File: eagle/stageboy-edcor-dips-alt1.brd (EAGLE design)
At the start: 120 x 75 mm, 35 parts, among them IC1 MEGA8-P, IC2 7805TV, J1 POWER_JACKPTH, Q1 16MHz, X1 MIDI IN, X2 MIDI OUT, X4 22-23-2021, X6 GBIO

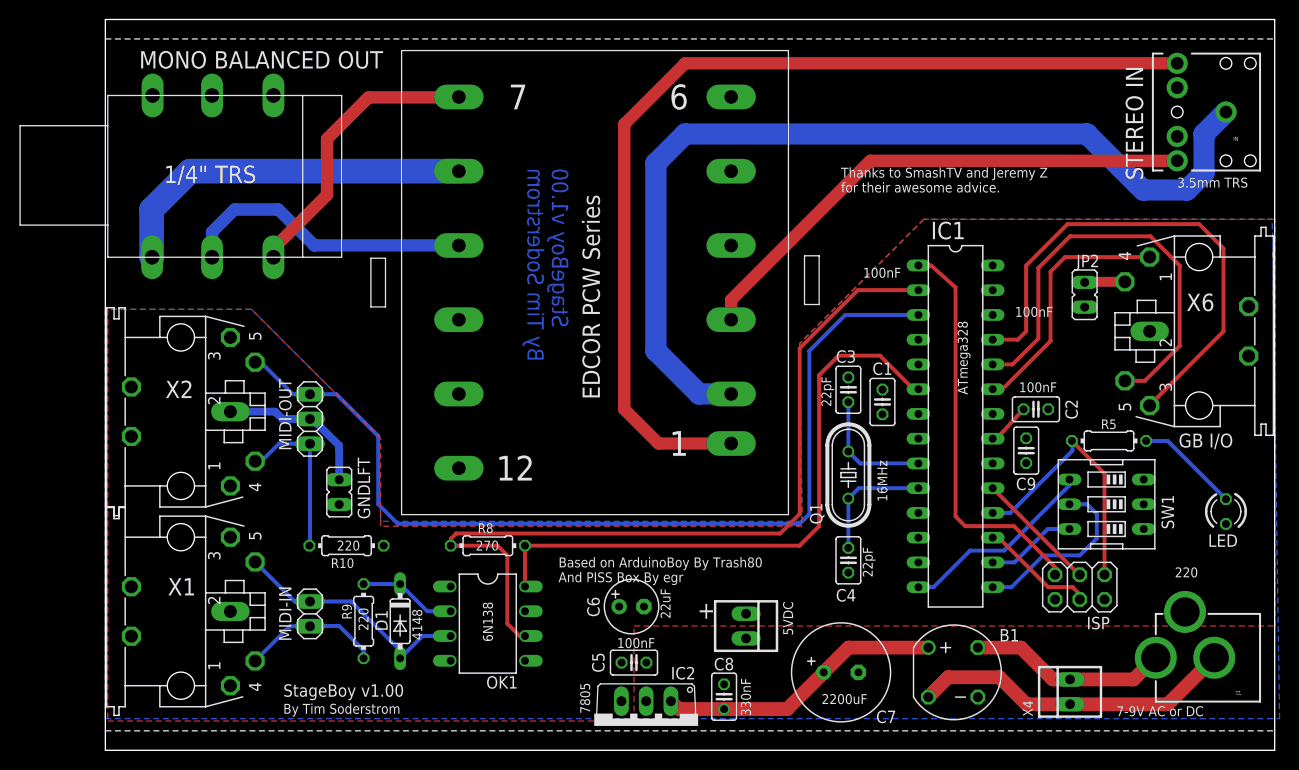
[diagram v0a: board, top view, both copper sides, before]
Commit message: Layout Changes
Extended PWR/GND planes
Moved the DIP switch around
Push the DC jack inwards to be flush-mounted to PCB
Other minor routing changes
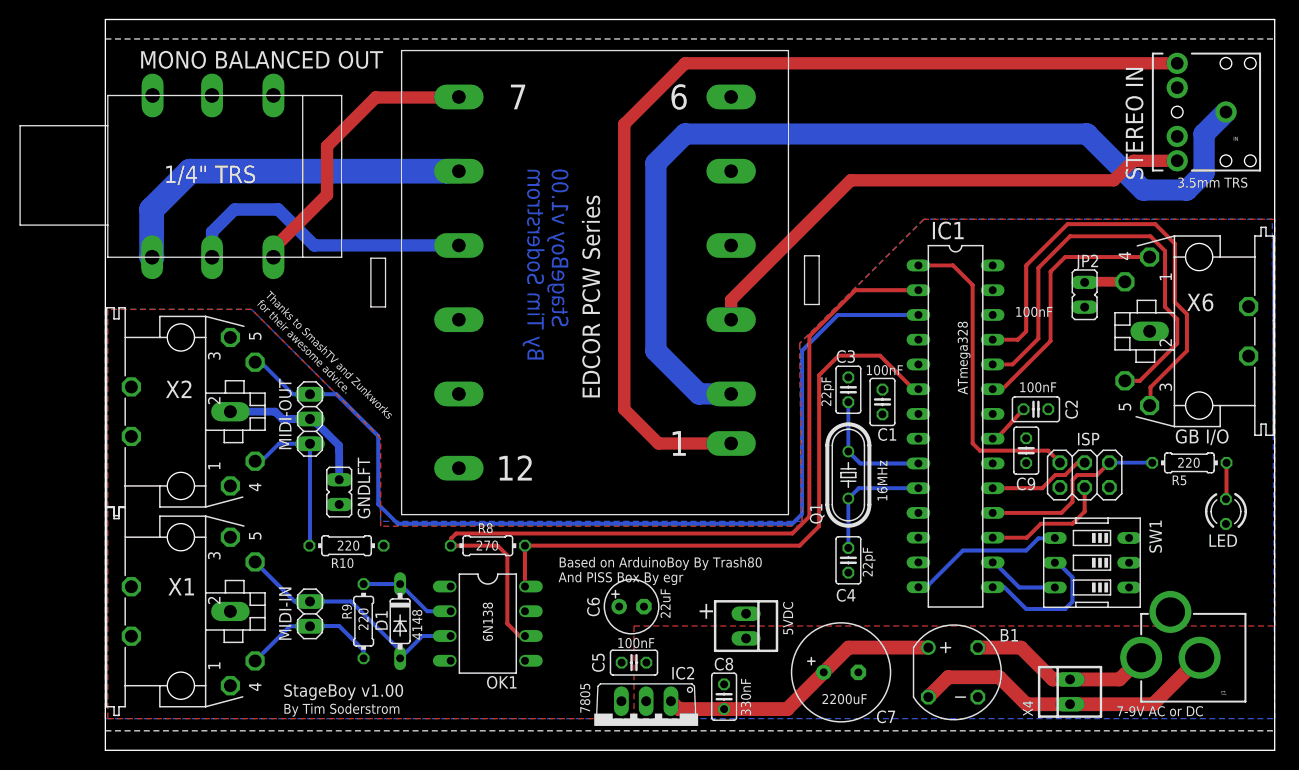
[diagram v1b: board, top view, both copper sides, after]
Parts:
- moved ISP 11.5 mm to (100.5, 28.2)
- moved R5 8.55 mm to (111.2, 29.5)
- moved SW1 6.18 mm to (101.2, 19.2)
- moved J1 1.50 mm to (120.0, 9.50)
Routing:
- net N$1: track 41.3 -> 32.4 mm
- net N$18: track 27.0 -> 19.8 mm
- net N$3: track 10.7 -> 3.75 mm
- net N$23: track 52.9 -> 47.1 mm
- net N$4: track 20.4 -> 15.8 mm
- net N$5: track 18.5 -> 14.4 mm
- net N$19: track 12.6 -> 10.5 mm
- net N$6: track 9.30 -> 7.44 mm
- net N$38: track 33.3 -> 31.8 mm
- net N$39: track 20.5 -> 19.0 mm
- net N$17: track 11.9 -> 13.0 mm
- net N$11: track 84.8 -> 85.7 mm
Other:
- board text added: "Thanks to SmashTV and Zunkworks for their awesome advice."
- board text removed: "Thanks to SmashTV and Jeremy Z for their awesome advice."

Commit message: Routing optimizations, Zip-Tie holes
Numerous routing changes / optimizations were made to help make the
best use of the ground and power planes for both power/gnd delivery
as well as isolation. On that note, the isolation on both planes
was lowered to 12 mil.

Added two more zip-tie holes. The cuts were not showing up on
the OshPark previews so I switched to using a line, which does show
up. Not enitrely show how well they exactly they will come out,
but I think the clearance is enough.
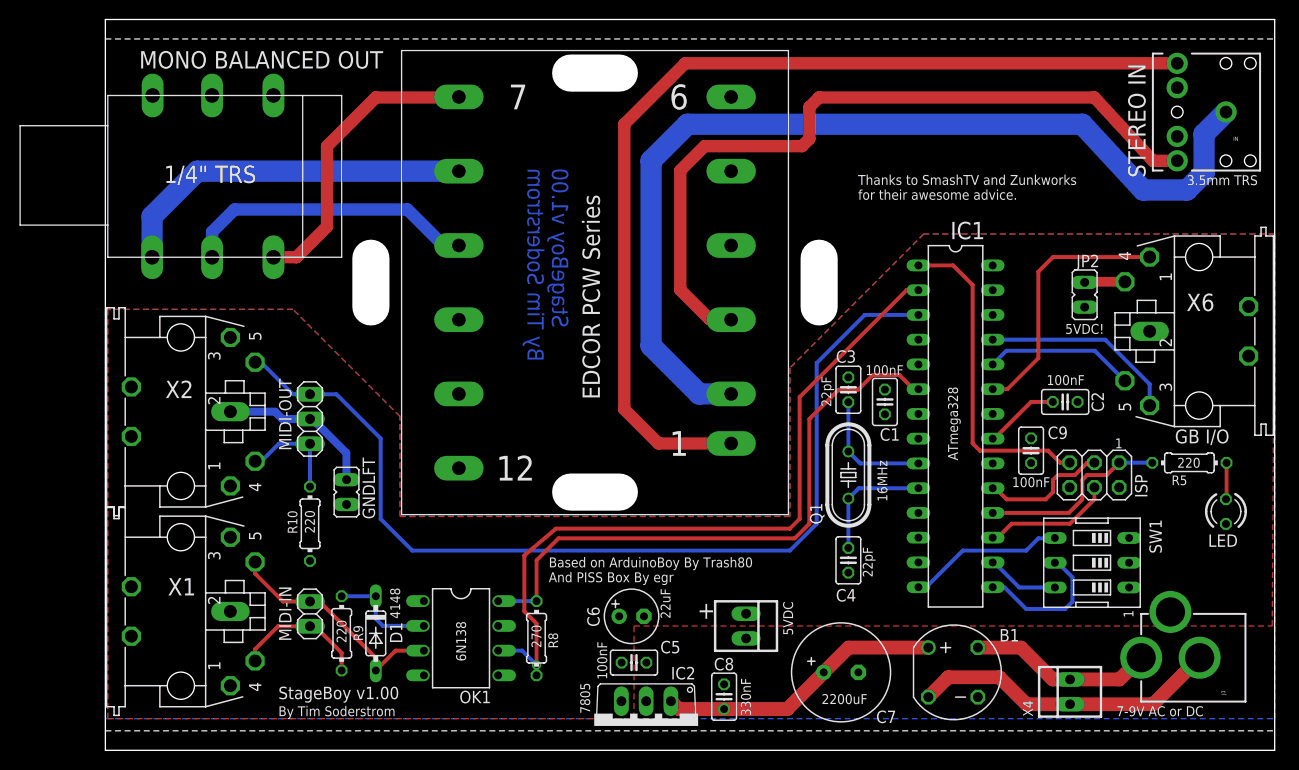
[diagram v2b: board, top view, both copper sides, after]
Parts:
- moved R8 10.7 mm to (44.2, 11.5), turned to 90 degrees
- moved R10 4.37 mm to (21.0, 23.2), turned to 90 degrees
- moved OK1 3.13 mm to (36.5, 11.5)
- moved C2 3.09 mm to (98.5, 35.8)
- moved D1 2.80 mm to (27.8, 12.0)
- moved R9 2.57 mm to (24.2, 12.0)
- moved C6 1.00 mm to (54.0, 13.8)
- moved ISP 1.00 mm to (101.5, 28.2)
- moved GNDLFT 0.75 mm to (24.8, 26.5)
- moved C9 0.50 mm to (95.0, 30.8)
- moved C1 0.25 mm to (80.0, 35.8)
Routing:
- net N$25: track 45.0 -> 15.4 mm
- net N$23: track 47.1 -> 20.2 mm
- net N$40: track 53.7 -> 77.6 mm
- net N$11: track 85.7 -> 76.3 mm, vias 0 -> 1
- net N$27: track 16.9 -> 10.8 mm
- net N$2: track 4.50 -> 7.73 mm
- net N$21: track 97.7 -> 100.6 mm
- net N$19: track 10.5 -> 13.2 mm
- net N$35: track 96.6 -> 98.4 mm
- net N$32: track 29.3 -> 30.7 mm
- net N$12: track 25.6 -> 24.2 mm
- net N$10: track 63.2 -> 62.1 mm
- net N$26: track 25.9 -> 26.9 mm
- net N$1: track 32.4 -> 33.4 mm
- net N$13: track 10.1 -> 11.1 mm
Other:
- outline, holes or cut-outs redrawn
- board text added: "1"
- board text added: "5VDC!"

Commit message: Rouge via...
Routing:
- net N$5: track 14.4 -> 13.7 mm
- net N$11: track 76.3 -> 76.7 mm, vias 1 -> 0
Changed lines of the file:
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@@
 <text x="47.5" y="59.75" size="1.6764" layer="16" font="vector" ratio="15" rot="MR270">StageBoy v1.00
 By Tim Soderstrom</text>
-<text x="17.75" y="5.25" size="1.27" layer="25" font="vector">StageBoy v1.00</text>
-<text x="17.75" y="3.5" size="1.016" layer="25" font="vector">By Tim Soderstrom</text>
+<text x="25" y="20.5" size="1.27" layer="25" font="vector">StageBoy v1.00</text>
+<text x="25" y="18.75" size="1.016" layer="25" font="vector">By Tim Soderstrom</text>
 <text x="45.5" y="17.25" size="1.016" layer="25" font="vector">Based on ArduinoBoy By Trash80
 And PISS Box By egr
@@
 <text x="104" y="31.5" size="1.016" layer="25" align="center">1</text>
 <text x="102.5" y="43.75" size="1.016" layer="25" rot="R180">5VDC!</text>
-<text x="105" y="14" size="1.016" layer="25" rot="R90" align="center">1</text>
+<text x="105" y="13.75" size="1.016" layer="25" rot="R180" align="center">1</text>
 <wire x1="27.25" y1="50.5" x2="27.25" y2="45.5" width="3.81" layer="20"/>
 <wire x1="52.75" y1="69.5" x2="47.75" y2="69.5" width="3.81" layer="20"/>
@@
 <contactref element="IC1" pad="2"/>
 <contactref element="R8" pad="1"/>
-<wire x1="40.31" y1="10.23" x2="42.77" y2="10.23" width="0.4064" layer="16"/>
-<wire x1="42.77" y1="10.23" x2="44.25" y2="8.75" width="0.4064" layer="16"/>
-<wire x1="44.25" y1="8.75" x2="44.25" y2="7.69" width="0.4064" layer="16"/>
-<via x="44.25" y="8.75" extent="1-16" drill="0.6" shape="square"/>
-<wire x1="44.25" y1="8.75" x2="44.25" y2="13" width="0.4064" layer="1"/>
 <wire x1="44.25" y1="13" x2="43" y2="14.25" width="0.4064" layer="1"/>
-<wire x1="43" y1="14.25" x2="43" y2="20" width="0.4064" layer="1"/>
-<wire x1="43" y1="20" x2="46.25" y2="22.75" width="0.4064" layer="1"/>
-<wire x1="46.25" y1="22.75" x2="70.25" y2="22.75" width="0.4064" layer="1"/>
-<wire x1="70.25" y1="22.75" x2="71.25" y2="23.75" width="0.4064" layer="1"/>
-<wire x1="71.25" y1="23.75" x2="71.25" y2="36.25" width="0.4064" layer="1"/>
-<wire x1="71.25" y1="36.25" x2="82.25" y2="47.25" width="0.4064" layer="1"/>
+<wire x1="43" y1="14.25" x2="43" y2="19.5" width="0.4064" layer="1"/>
+<wire x1="43" y1="19.5" x2="46.25" y2="22.75" width="0.4064" layer="1"/>
+<wire x1="46.25" y1="22.75" x2="70.5" y2="22.75" width="0.4064" layer="1"/>
+<wire x1="70.5" y1="22.75" x2="71.5" y2="23.75" width="0.4064" layer="1"/>
+<wire x1="71.5" y1="23.75" x2="71.5" y2="36.5" width="0.4064" layer="1"/>
+<wire x1="71.5" y1="36.5" x2="82.25" y2="47.25" width="0.4064" layer="1"/>
 <wire x1="82.25" y1="47.25" x2="83.41" y2="47.25" width="0.4064" layer="1"/>
 <wire x1="83.41" y1="47.25" x2="83.44" y2="47.22" width="0.4064" layer="1"/>
+<wire x1="44.25" y1="13" x2="44.25" y2="7.69" width="0.4064" layer="1"/>
+<wire x1="40.31" y1="10.23" x2="41.71" y2="10.23" width="0.4064" layer="16"/>
+<wire x1="41.71" y1="10.23" x2="44.25" y2="7.69" width="0.4064" layer="16"/>
 </signal>
 <signal name="N$12">
@@
 <wire x1="91.06" y1="21.82" x2="91.57" y2="21.82" width="0.4064" layer="1"/>
 <wire x1="91.57" y1="21.82" x2="93" y2="23.25" width="0.4064" layer="1"/>
-<wire x1="93" y1="23.25" x2="99" y2="23.25" width="0.4064" layer="1"/>
-<wire x1="99" y1="23.25" x2="101.5" y2="25.75" width="0.4064" layer="1"/>
-<wire x1="101.5" y1="25.75" x2="101.5" y2="26.98" width="0.4064" layer="1"/>
+<wire x1="93" y1="23.25" x2="99.25" y2="23.25" width="0.4064" layer="1"/>
+<wire x1="99.25" y1="23.25" x2="101.5" y2="25.5" width="0.4064" layer="1"/>
+<wire x1="101.5" y1="25.5" x2="101.5" y2="26.98" width="0.4064" layer="1"/>
 </signal>
 <signal name="N$18">
@@
 <contactref element="IC1" pad="1"/>
 <contactref element="ISP" pad="5"/>
-<wire x1="97.98" y1="29.52" x2="96.75" y2="30.75" width="0.4064" layer="1"/>
-<wire x1="96.75" y1="30.75" x2="89.75" y2="30.75" width="0.4064" layer="1"/>
+<wire x1="98.98" y1="29.52" x2="97.75" y2="30.75" width="0.4064" layer="1"/>
+<wire x1="97.75" y1="30.75" x2="89.75" y2="30.75" width="0.4064" layer="1"/>
 <wire x1="89.75" y1="30.75" x2="89" y2="31.5" width="0.4064" layer="1"/>
 <wire x1="89" y1="31.5" x2="89" y2="47.75" width="0.4064" layer="1"/>
 <wire x1="89" y1="47.75" x2="86.99" y2="49.76" width="0.4064" layer="1"/>
 <wire x1="83.44" y1="49.76" x2="86.99" y2="49.76" width="0.4064" layer="1"/>
-<wire x1="98.96" y1="29.52" x2="97.98" y2="29.52" width="0.4064" layer="1"/>
+<wire x1="98.96" y1="29.52" x2="98.98" y2="29.52" width="0.4064" layer="1"/>
 </signal>
 <signal name="N$35">
@@
 <contactref element="IC1" pad="15"/>
 <wire x1="91.06" y1="16.74" x2="92.26" y2="16.74" width="0.4064" layer="16"/>
-<wire x1="92.26" y1="16.74" x2="94.5" y2="14.5" width="0.4064" layer="16"/>
-<wire x1="94.5" y1="14.5" x2="98.5" y2="14.5" width="0.4064" layer="16"/>
-<wire x1="98.5" y1="14.5" x2="99.25" y2="15.25" width="0.4064" layer="16"/>
-<wire x1="99.25" y1="15.25" x2="99.25" y2="17.75" width="0.4064" layer="16"/>
+<wire x1="92.26" y1="16.74" x2="94" y2="15" width="0.4064" layer="16"/>
+<wire x1="94" y1="15" x2="98.5" y2="15" width="0.4064" layer="16"/>
+<wire x1="98.5" y1="15" x2="99.25" y2="15.75" width="0.4064" layer="16"/>
+<wire x1="99.25" y1="15.75" x2="99.25" y2="17.75" width="0.4064" layer="16"/>
 <wire x1="99.25" y1="17.75" x2="97.75" y2="19.25" width="0.4064" layer="16"/>
 <wire x1="97.75" y1="19.25" x2="97.44" y2="19.25" width="0.4064" layer="16"/>
